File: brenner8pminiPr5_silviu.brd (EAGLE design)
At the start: 82.5 x 42.4 mm, 39 parts, among them IC1 PIC18F2550SP, Q1 20 MHz, Q2 BC338-25, Q3 BC338-25, Q4 BC328-25, Q5 BC328-25, Q6 BF959, X2 USB-B-H

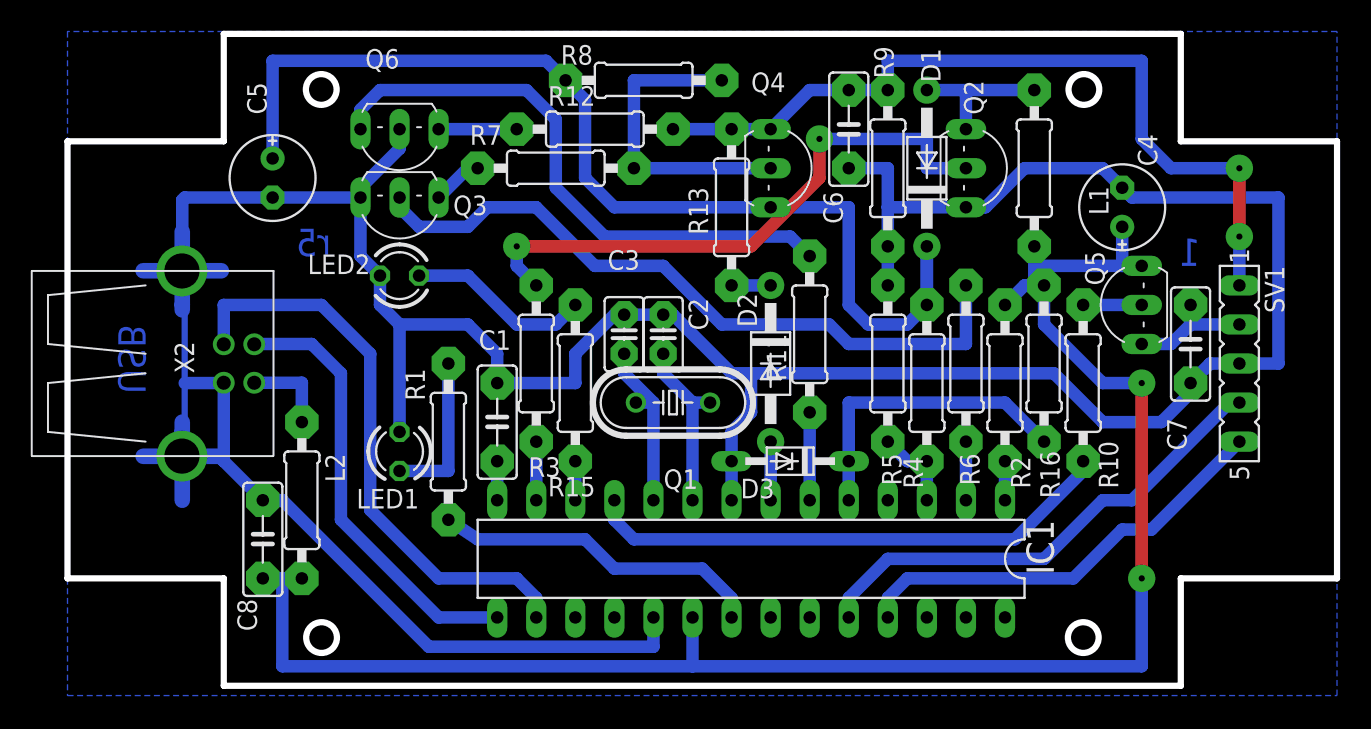
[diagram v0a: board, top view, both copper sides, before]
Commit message: Fixed via sizes. Vias for mounting holes. DRC fixes
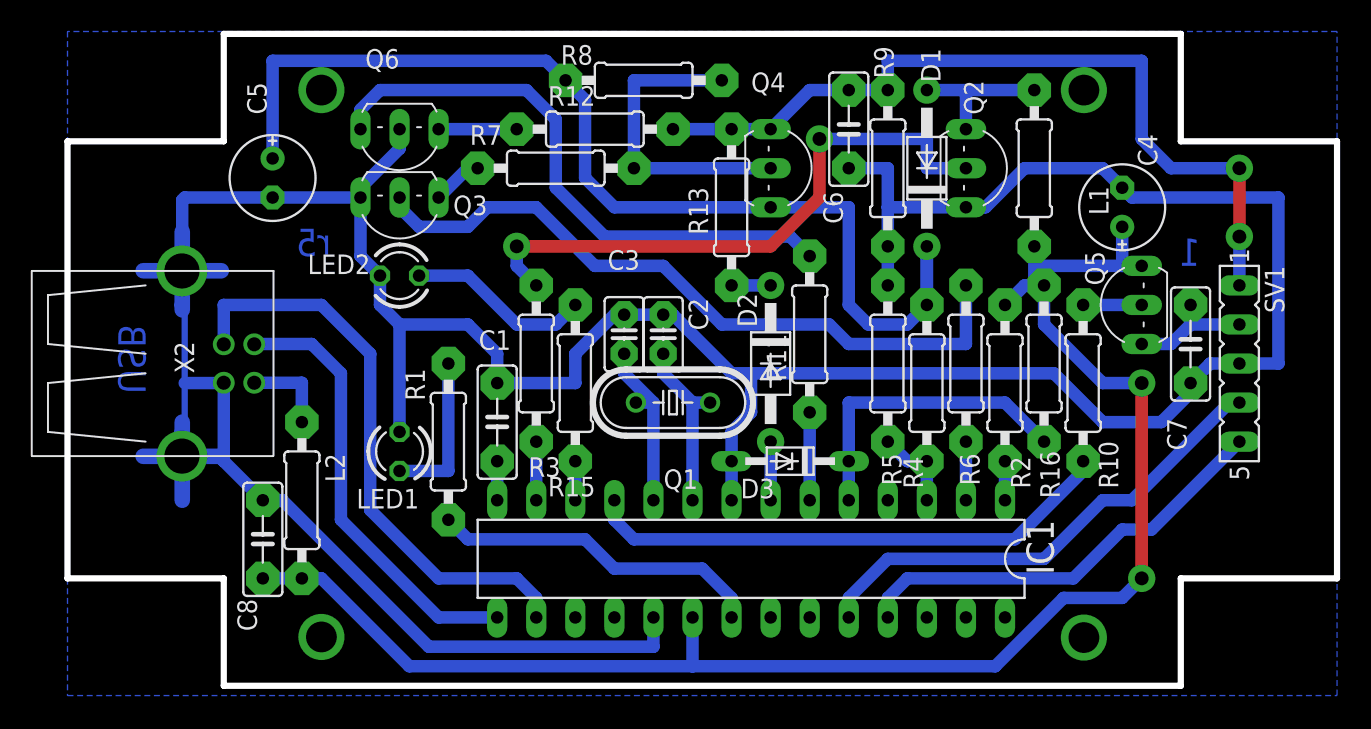
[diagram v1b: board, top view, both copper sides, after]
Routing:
- net VDD: track 112.0 -> 104.0 mm
- net N$14: track 38.6 -> 39.3 mm
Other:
- outline, holes or cut-outs redrawn
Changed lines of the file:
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@@
 <setting verticaltext="up"/>
 </settings>
-<grid distance="100" unitdist="mil" unit="mil" style="dots" multiple="1" display="yes" altdistance="6.25" altunitdist="mil" altunit="inch"/>
+<grid distance="25" unitdist="mil" unit="mil" style="dots" multiple="1" display="yes" altdistance="6.25" altunitdist="mil" altunit="inch"/>
 <layers>
 <layer number="1" name="Top" color="4" fill="1" visible="yes" active="yes"/>
@@
 <wire x1="82.55" y1="34.77" x2="72.39" y2="34.77" width="0.4064" layer="20"/>
 <wire x1="82.55" y1="6.35" x2="72.39" y2="6.35" width="0.4064" layer="20"/>
-<circle x="16.52" y="2.5" radius="1" width="0.4064" layer="20"/>
-<circle x="16.5" y="38.14" radius="1" width="0.4064" layer="20"/>
-<circle x="66.09" y="38.14" radius="1" width="0.4064" layer="20"/>
-<circle x="66.05" y="2.5" radius="1" width="0.4064" layer="20"/>
 <circle x="27.94" y="13.97" radius="0.303" width="0.206" layer="116"/>
 <circle x="27.94" y="19.05" radius="0.303" width="0.206" layer="116"/>
@@
 <circle x="24.765" y="20.32" radius="0.303" width="0.206" layer="116"/>
 <circle x="24.765" y="10.16" radius="0.303" width="0.206" layer="116"/>
-<text x="5.08" y="22.86" size="1.778" layer="16" rot="MR270">USB</text>
-<text x="17.145" y="27.305" size="1.778" layer="16" rot="MR0">r5</text>
-<text x="73.66" y="26.67" size="1.778" layer="16" rot="MR0">1</text>
+<text x="5.08" y="22.86" size="1.778" layer="16" font="vector" ratio="15" rot="MR270">USB</text>
+<text x="17.145" y="27.305" size="1.778" layer="16" font="vector" ratio="15" rot="MR0">r5</text>
+<text x="73.66" y="26.67" size="1.778" layer="16" font="vector" ratio="15" rot="MR0">1</text>
 </plain>
 <attributes>
@@
 <wire x1="55.88" y1="34.925" x2="55.88" y2="33.02" width="0.8128" layer="16"/>
 <wire x1="48.895" y1="34.925" x2="55.88" y2="34.925" width="0.8128" layer="16"/>
-<wire x1="29.21" y1="27.94" x2="44.45" y2="27.94" width="0.8128" layer="1"/>
-<wire x1="44.45" y1="27.94" x2="48.895" y2="32.385" width="0.8128" layer="1"/>
-<wire x1="48.895" y1="32.385" x2="48.895" y2="34.925" width="0.8128" layer="1"/>
+<wire x1="29.21" y1="27.94" x2="45.72" y2="27.94" width="0.8128" layer="1"/>
+<wire x1="45.72" y1="27.94" x2="48.895" y2="31.115" width="0.8128" layer="1"/>
+<wire x1="48.895" y1="31.115" x2="48.895" y2="34.925" width="0.8128" layer="1"/>
 <wire x1="29.21" y1="26.67" x2="29.21" y2="27.94" width="0.8128" layer="16"/>
 <wire x1="29.21" y1="26.67" x2="30.48" y2="25.4" width="0.8128" layer="16"/>
-<via x="48.895" y="34.925" extent="1-16" drill="0.4" diameter="1.778"/>
-<via x="29.21" y="27.94" extent="1-16" drill="0.4" diameter="1.778"/>
+<via x="48.895" y="34.925" extent="1-16" drill="0.9" diameter="1.778"/>
+<via x="29.21" y="27.94" extent="1-16" drill="0.9" diameter="1.778"/>
 </signal>
 <signal name="N$15">
@@
 <wire x1="45.72" y1="35.56" x2="48.26" y2="38.1" width="0.8128" layer="16"/>
 <wire x1="48.26" y1="38.1" x2="50.8" y2="38.1" width="0.8128" layer="16"/>
-<via x="76.2" y="28.575" extent="1-16" drill="0.4" diameter="1.778"/>
-<via x="76.2" y="33.02" extent="1-16" drill="0.4" diameter="1.778"/>
+<via x="76.2" y="28.575" extent="1-16" drill="0.9" diameter="1.778"/>
+<via x="76.2" y="33.02" extent="1-16" drill="0.9" diameter="1.778"/>
 </signal>
 <signal name="N$28">
@@
 <contactref element="R1" pad="1"/>
 <contactref element="IC1" pad="21"/>
-<wire x1="24.765" y1="10.16" x2="26.67" y2="8.89" width="0.8128" layer="16"/>
-<wire x1="26.67" y1="8.89" x2="33.655" y2="8.89" width="0.8128" layer="16"/>
+<wire x1="24.765" y1="10.16" x2="26.035" y2="8.89" width="0.8128" layer="16"/>
+<wire x1="26.035" y1="8.89" x2="33.655" y2="8.89" width="0.8128" layer="16"/>
 <wire x1="33.655" y1="8.89" x2="35.56" y2="6.985" width="0.8128" layer="16"/>
 <wire x1="35.56" y1="6.985" x2="41.275" y2="6.985" width="0.8128" layer="16"/>
@@
 <wire x1="68.58" y1="26.67" x2="69.85" y2="26.67" width="0.8128" layer="16"/>
 <wire x1="69.85" y1="6.35" x2="69.85" y2="19.05" width="0.8128" layer="1"/>
-<wire x1="69.85" y1="0.635" x2="69.85" y2="6.35" width="0.8128" layer="16"/>
-<wire x1="40.64" y1="0.635" x2="69.85" y2="0.635" width="0.8128" layer="16"/>
+<wire x1="68.58" y1="5.08" x2="69.85" y2="6.35" width="0.8128" layer="16"/>
+<wire x1="40.64" y1="0.635" x2="60.325" y2="0.635" width="0.8128" layer="16"/>
+<wire x1="60.325" y1="0.635" x2="64.77" y2="5.08" width="0.8128" layer="16"/>
+<wire x1="64.77" y1="5.08" x2="68.58" y2="5.08" width="0.8128" layer="16"/>
 <wire x1="69.85" y1="19.05" x2="67.31" y2="19.05" width="0.8128" layer="16"/>
 <wire x1="67.31" y1="19.05" x2="63.5" y2="22.86" width="0.8128" layer="16"/>
 <wire x1="63.5" y1="22.86" x2="63.5" y2="25.4" width="0.8128" layer="16"/>
 <wire x1="40.64" y1="0.635" x2="40.64" y2="3.81" width="0.8128" layer="16"/>
-<wire x1="13.97" y1="0.635" x2="40.64" y2="0.635" width="0.8128" layer="16"/>
-<wire x1="13.97" y1="0.635" x2="13.97" y2="6.35" width="0.8128" layer="16"/>
-<wire x1="13.97" y1="6.35" x2="12.7" y2="6.35" width="0.8128" layer="16"/>
-<wire x1="13.97" y1="6.35" x2="15.24" y2="6.35" width="0.8128" layer="16"/>
-<via x="69.85" y="19.05" extent="1-16" drill="0.4" diameter="1.778"/>
-<via x="69.85" y="6.35" extent="1-16" drill="0.4" diameter="1.778"/>
+<wire x1="22.225" y1="0.635" x2="40.64" y2="0.635" width="0.8128" layer="16"/>
+<via x="69.85" y="19.05" extent="1-16" drill="0.9" diameter="1.778"/>
+<via x="69.85" y="6.35" extent="1-16" drill="0.9" diameter="1.778"/>
+<wire x1="22.225" y1="0.635" x2="16.51" y2="6.35" width="0.8128" layer="16"/>
+<wire x1="16.51" y1="6.35" x2="15.24" y2="6.35" width="0.8128" layer="16"/>
+<wire x1="15.24" y1="6.35" x2="12.7" y2="6.35" width="0.8128" layer="16"/>
 </signal>
 <signal name="VSS">
@@
 </polygon>
 </signal>
+<signal name="N$29">
+<via x="16.51" y="2.54" extent="1-16" drill="2"/>
+<via x="16.51" y="38.1" extent="1-16" drill="2"/>
+<via x="66.09" y="38.1" extent="1-16" drill="2"/>
+<via x="66.09" y="2.5" extent="1-16" drill="2"/>
+</signal>
 </signals>

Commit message: Reorder components and fix DRC errors
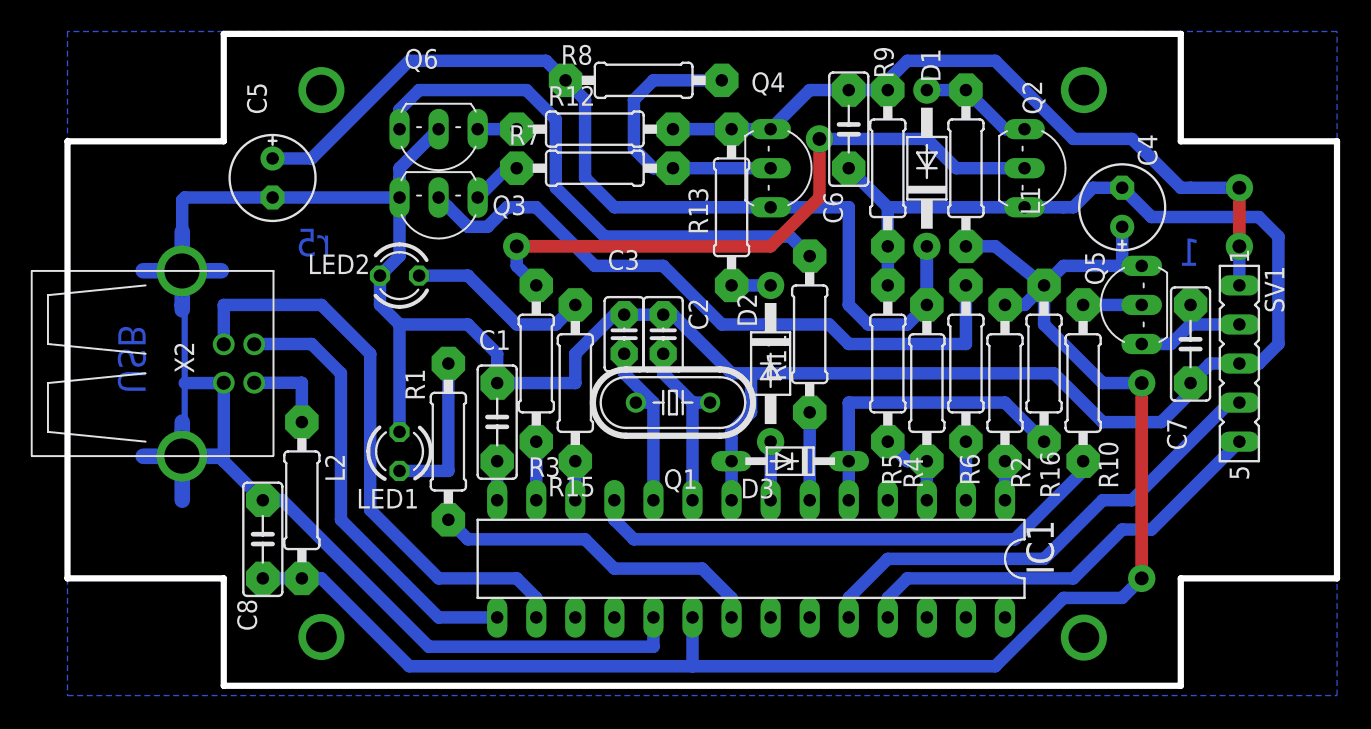
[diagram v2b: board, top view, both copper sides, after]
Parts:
- moved L1 4.45 mm to (58.4, 33.0)
- moved Q2 3.81 mm to (63.5, 33.0)
- moved Q3 2.54 mm to (24.1, 29.8)
- moved Q6 2.54 mm to (24.1, 35.6)
- moved R7 2.54 mm to (34.3, 33.0)
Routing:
- net VPP_8_14_18: track 53.3 -> 48.8 mm
- net +12V: track 70.8 -> 67.1 mm
- net N$21: track 46.0 -> 43.1 mm
- net N$14: track 39.3 -> 42.0 mm
- net VDD: track 104.0 -> 106.7 mm
- net N$22: track 5.08 -> 2.54 mm
- net N$19: track 38.1 -> 35.5 mm
- net VSS: track 234.1 -> 231.9 mm
- net N$13: track 9.52 -> 7.40 mm
- net N$24: track 20.3 -> 18.8 mm

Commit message: Smaller cap footprint
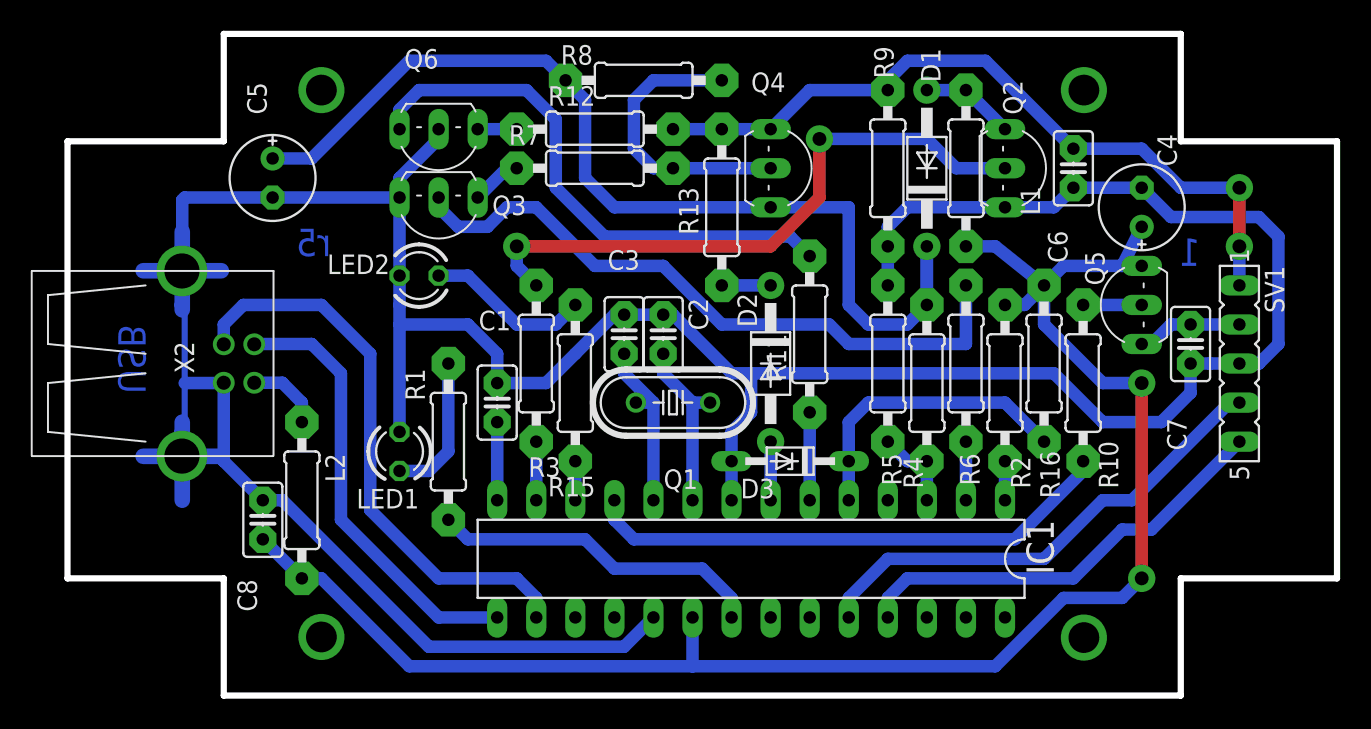
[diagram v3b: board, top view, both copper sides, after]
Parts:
- C1, C6, C7, C8: device rcl:C050-025X075 -> rcl:C025-025X050
- moved C6 14.8 mm to (65.4, 33.0)
- moved Q2 1.27 mm to (62.2, 33.0)
- moved C1 1.27 mm to (27.9, 17.8)
- moved C8 1.27 mm to (12.7, 10.2)
- moved LED2 1.27 mm to (22.9, 26.0)
- moved C4 1.27 mm to (69.8, 30.5)
- moved R13 0.63 mm to (42.5, 30.5)
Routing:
- net VSS: track 231.9 -> 225.0 mm
- net N$5: track 2.54 -> 5.08 mm
- net VDD: track 106.7 -> 108.0 mm
- net N$12: track 12.0 -> 10.7 mm
- net N$14: track 42.0 -> 40.7 mm
- net N$13: track 7.40 -> 6.13 mm
- net N$17: track 8.15 -> 6.88 mm
- net N$3: track 5.66 -> 4.91 mm
- net N$4: track 10.2 -> 9.42 mm
- net UREF: track 20.1 -> 19.4 mm
- net N$2: track 38.0 -> 37.2 mm
- net N$26: track 2.54 -> 3.17 mm
- removed copper zone on layer 16, net VSS
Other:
- board size 82.5 x 42.4 mm -> 82.5 x 43 mm

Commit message: Reduced pad sizes
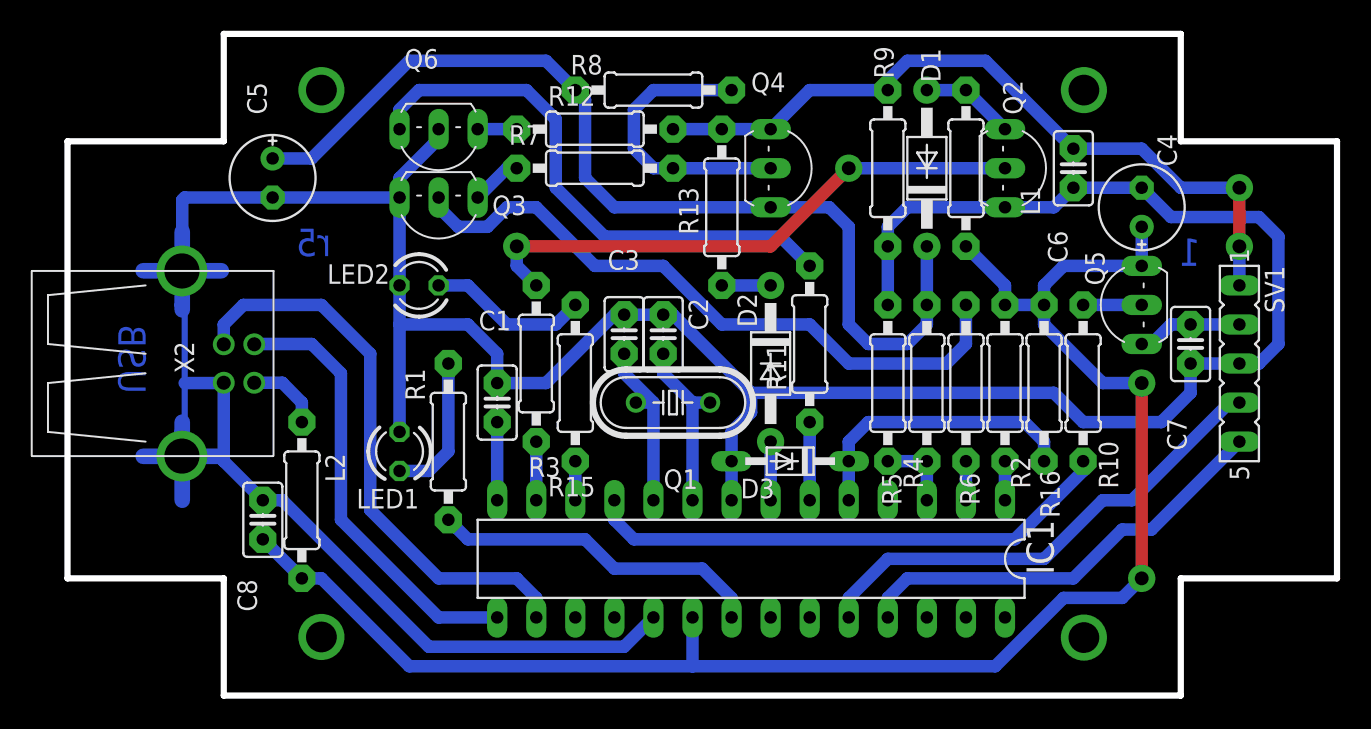
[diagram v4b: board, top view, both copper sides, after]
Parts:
- moved R16 1.27 mm to (63.5, 19.1)
- moved R5 1.27 mm to (53.3, 19.1)
- moved R6 1.27 mm to (58.4, 19.1)
- moved R8 0.90 mm to (38.1, 38.1)
- moved LED2 0.64 mm to (22.9, 25.4)
- moved R11 0.64 mm to (48.3, 21.6)
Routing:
- net N$14: track 40.7 -> 36.9 mm
- net +12V: track 67.1 -> 65.1 mm
- net VDD: track 108.0 -> 106.1 mm
- net N$28: track 3.81 -> 2.54 mm
- net N$20: track 5.71 -> 5.08 mm
- net UREF: track 19.4 -> 18.8 mm
- net N$18: track 5.61 -> 5.08 mm

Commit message: Snap components to grid 50. Labels fix
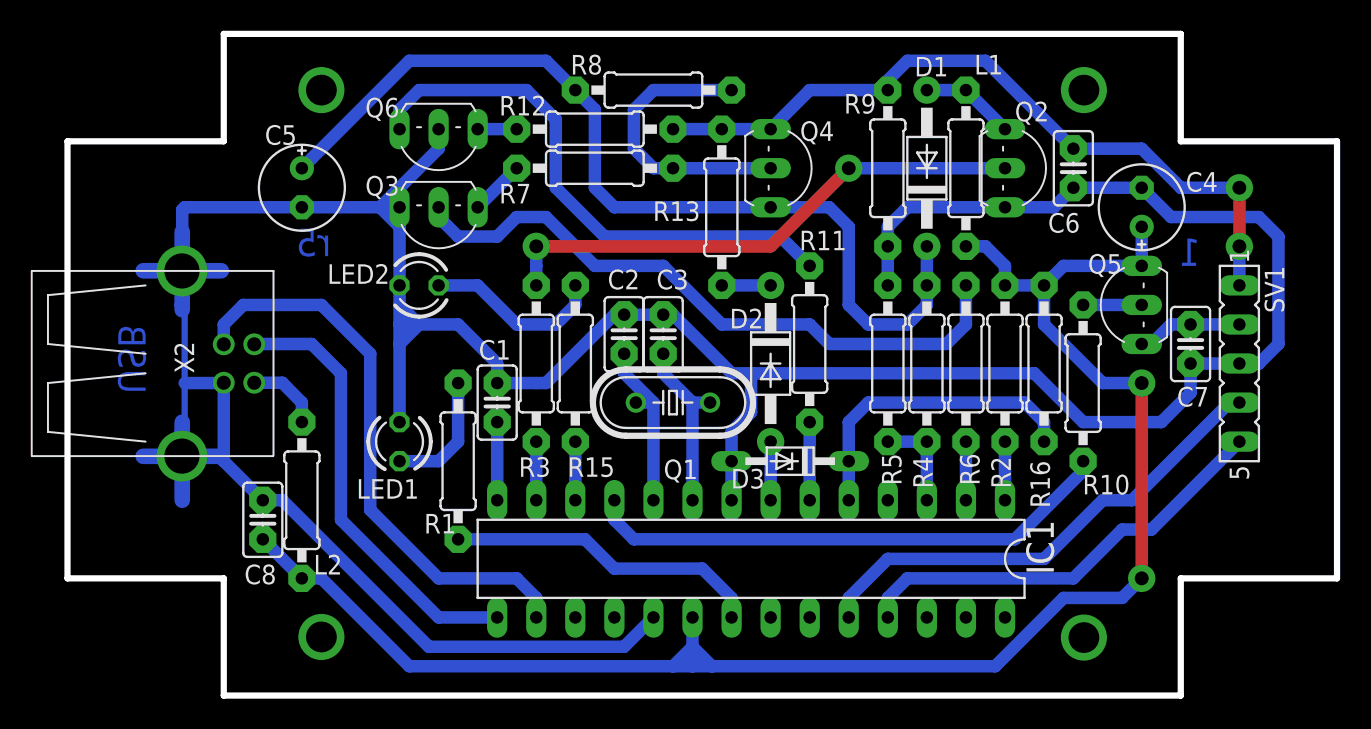
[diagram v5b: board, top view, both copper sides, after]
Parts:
- moved C5 2.01 mm to (15.2, 31.8)
- moved R1 1.42 mm to (25.4, 14.0)
- moved R15 1.27 mm to (33.0, 20.3)
- moved R16 1.27 mm to (63.5, 20.3)
- moved R2 1.27 mm to (61.0, 20.3)
- moved R4 1.27 mm to (55.9, 20.3)
- moved R5 1.27 mm to (53.3, 20.3)
- moved R6 1.27 mm to (58.4, 20.3)
- moved LED1 0.63 mm to (21.6, 15.2)
- moved Q3 0.63 mm to (24.1, 29.2)
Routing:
- net VSS: track 225.0 -> 232.3 mm
- net +12V: track 65.1 -> 60.9 mm
- net VDD: track 106.1 -> 109.2 mm
- net N$14: track 36.9 -> 35.1 mm
- net UREF: track 18.8 -> 20.1 mm
- net N$4: track 9.42 -> 8.15 mm
- net N$8: track 2.54 -> 3.81 mm
- net N$28: track 2.54 -> 3.81 mm
- net N$18: track 5.08 -> 6.35 mm
- net N$12: track 10.5 -> 11.7 mm
- net N$10: track 2.54 -> 3.81 mm
- net N$16: track 21.8 -> 20.6 mm
- net N$21: track 43.3 -> 42.5 mm
